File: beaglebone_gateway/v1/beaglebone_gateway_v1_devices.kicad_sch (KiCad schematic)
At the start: 27 parts, among them J1 PWR_CONNECTOR, J2 BATT CURENT SENSING, J3 EXT_I2C, J4 EXT_UART, U1 RA-02_LORA, U2 ACS725xLCTR-10AU, U3 BME280, U4 R-78B5.0-2.0

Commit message: Remove comments, add sheets description
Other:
- note added: "Beaglebone Black LoRa gateway HAT."
- note added: "Beaglebone Black LoRa gateway HAT. Buzzverse. Authors: Jakub Martyński Maciej Wołosewicz"
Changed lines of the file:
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@@
+    (effects (font (size 1.27 1.27)) (justify left bottom))
+  )
+  (text "Beaglebone Black LoRa gateway HAT. Buzzverse.\n\nAuthors:\nJakub Martyński\nMaciej Wołosewicz"
+    (at 177.8 177.8 0)
     (effects (font (size 1.27 1.27)) (justify left bottom))
   )
@@
     (effects (font (size 1.27 1.27)) (justify left bottom))
   )
+  (text "Beaglebone Black LoRa gateway HAT." (at 186.69 190.5 0)
+    (effects (font (size 1.27 1.27) (color 9 0 241 1)) (justify left bottom))
+  )
   (text "CSB must be VDDIO\nto enable I2C." (at 220.98 35.56 0)

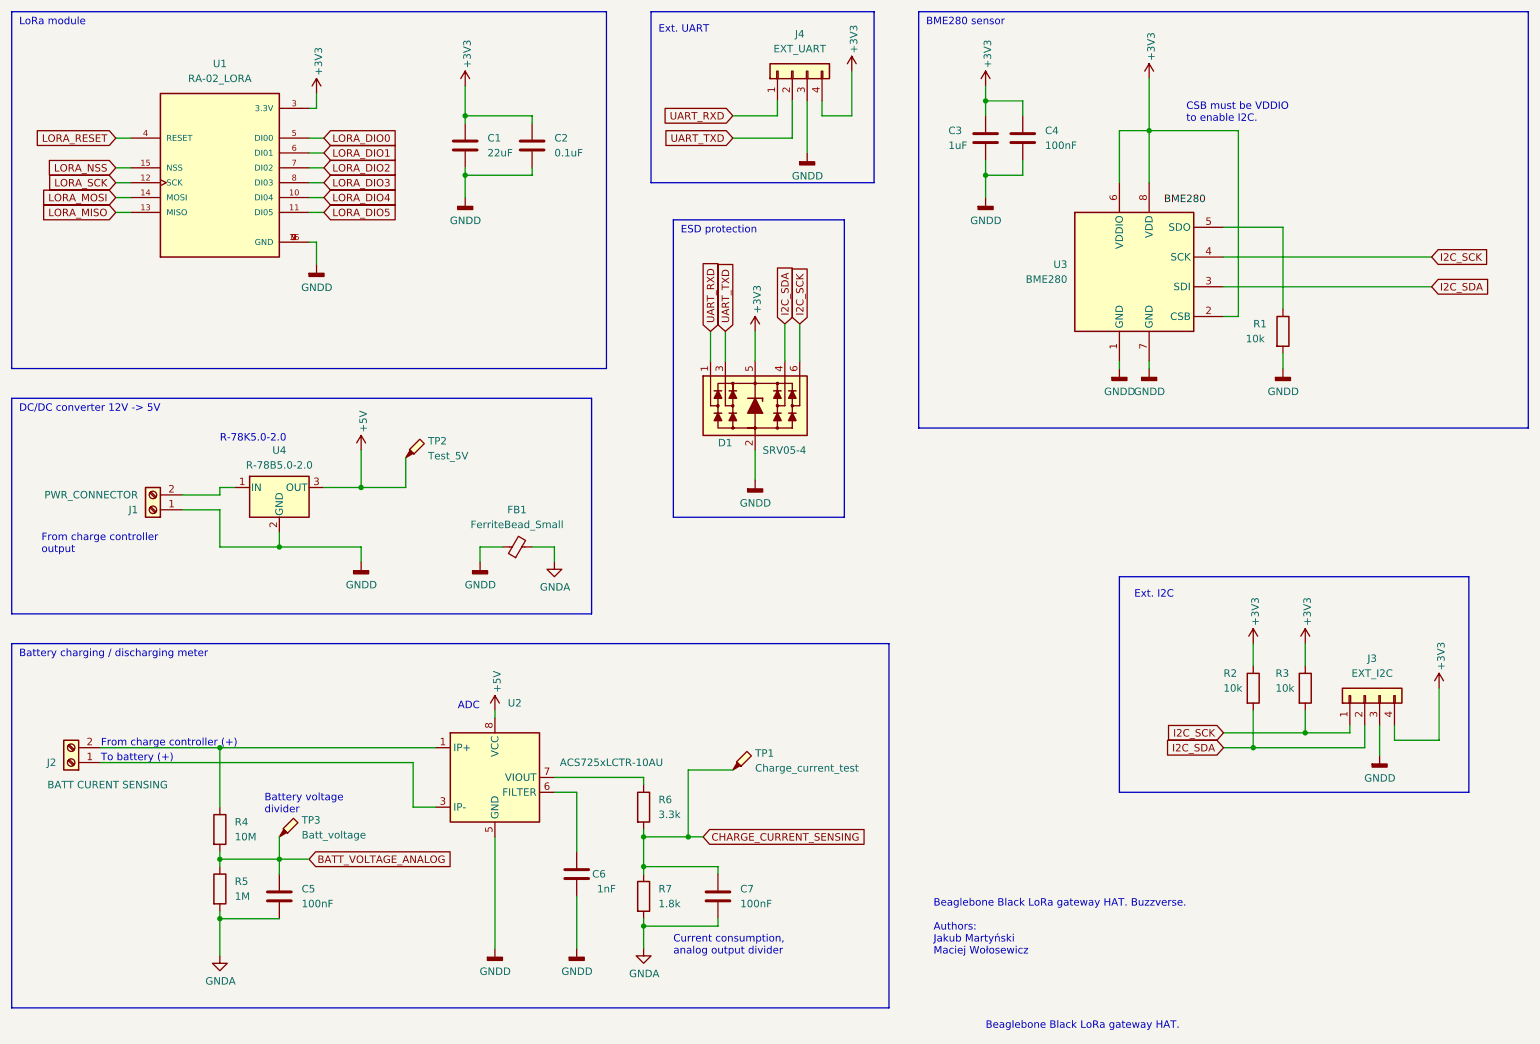
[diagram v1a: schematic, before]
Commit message: Add ADC divider cut off using complementary mosfet transistors
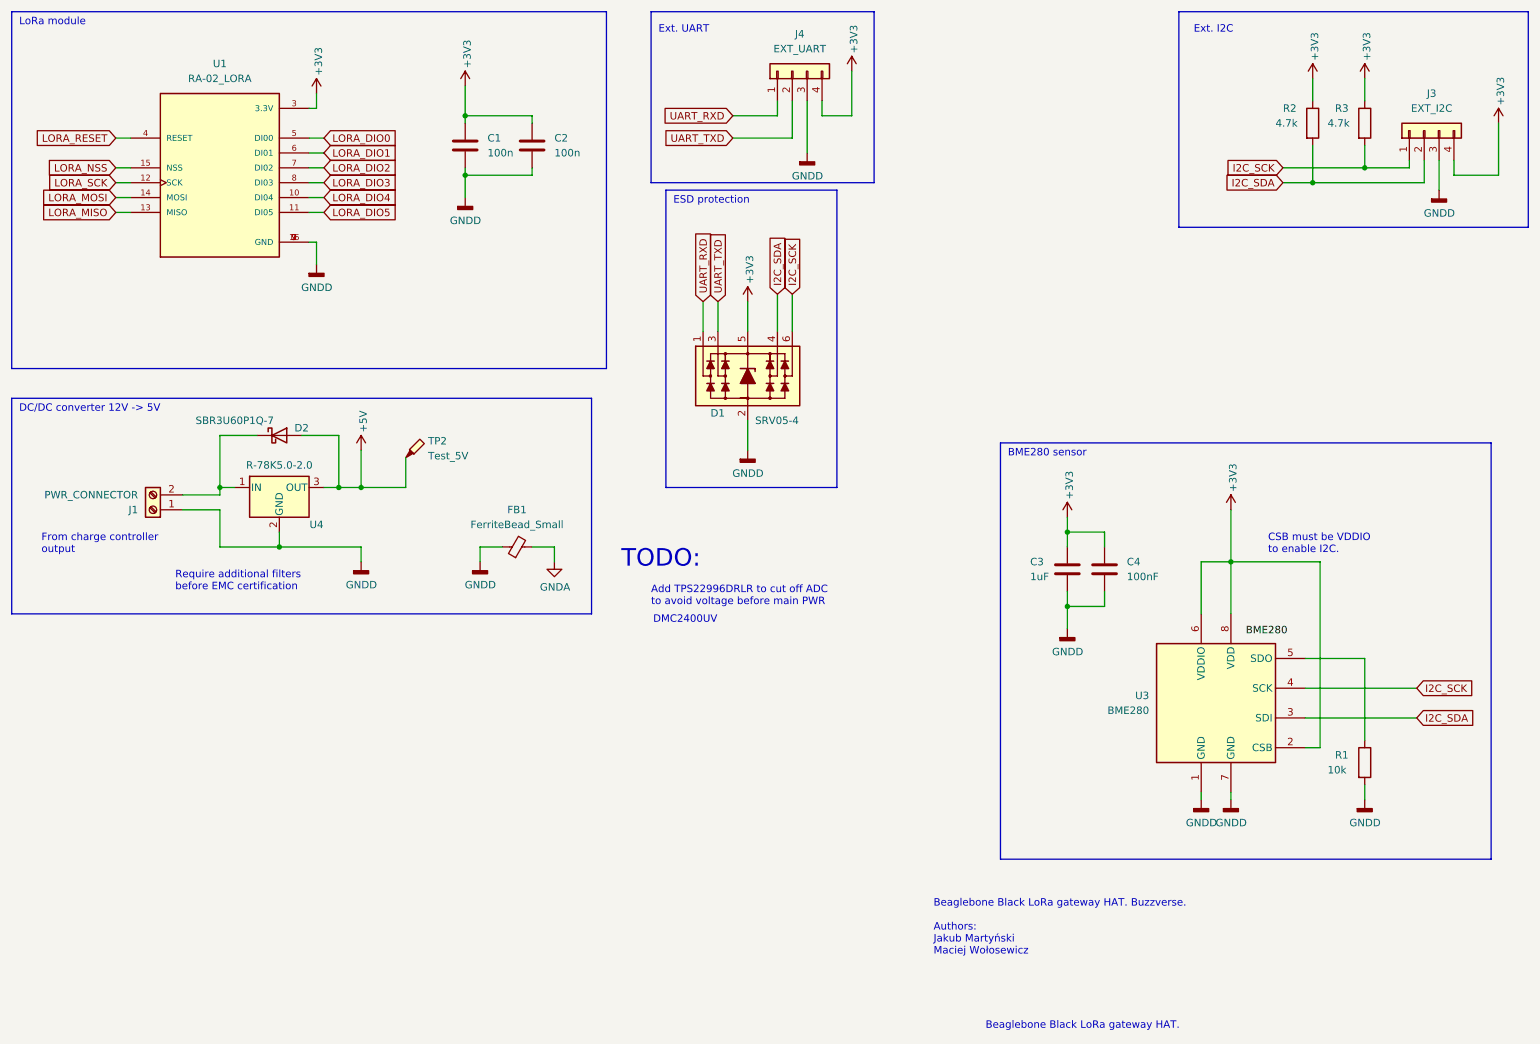
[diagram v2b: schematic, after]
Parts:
- removed C5, C7: 100nF, Capacitor_SMD:C_0603_1608Metric, symbol Device:C
- removed C6: 1nF, Capacitor_SMD:C_0603_1608Metric, symbol Device:C
- removed J2: BATT CURENT SENSING, TerminalBlock_Phoenix:TerminalBlock_Phoenix_PT-1,5-2-3.5-H_1x02_P3.50mm_Horizontal, symbol Connector:Screw_Terminal_01x02
- removed R4: 10M, Resistor_SMD:R_0603_1608Metric, symbol Device:R
- removed R5: 1M, Resistor_SMD:R_0603_1608Metric, symbol Device:R
- removed R6: 3.3k, Resistor_SMD:R_0603_1608Metric, symbol Device:R
- removed R7: 1.8k, Resistor_SMD:R_0603_1608Metric, symbol Device:R
- removed TP1: Charge_current_test, TestPoint:TestPoint_Pad_D1.5mm, symbol Connector:TestPoint_Probe
- removed TP3: Batt_voltage, TestPoint:TestPoint_Pad_D1.5mm, symbol Connector:TestPoint_Probe
- removed U2: ACS725xLCTR-10AU, Package_SO:SOIC-8_3.9x4.9mm_P1.27mm, symbol Sensor_Current:ACS725xLCTR-10AU
- added D2: SBR3U60P1Q-7, Diode_SMD:D_PowerDI-123, symbol Device:D_Schottky
- C1: value 22uF -> 100n
- C2: value 0.1uF -> 100n
- R2, R3: value 10k -> 4.7k
- U4: value R-78B5.0-2.0 -> R-78K5.0-2.0
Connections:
- net +5V: now also D2.2 (A)
- net at J1.2 (Pin_2), U4.1 (IN): now also D2.1 (K)
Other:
- note added: "Add TPS22996DRLR to cut off ADC to avoid voltage before main PWR"
- note added: "DMC2400UV"
- note added: "Require additional filters before EMC certification"
- note added: "TODO:"
- note removed: "ADC"
- note removed: "Battery charging / discharging meter"
- note removed: "Battery voltage divider"
- note removed: "Current consumption, analog output divider"
- note removed: "From charge controller (+)"
- note removed: "R-78K5.0-2.0"
- note removed: "To battery (+)"
- moved on the sheet: C3, C4, D1, J3, R1, R2, R3, U3
